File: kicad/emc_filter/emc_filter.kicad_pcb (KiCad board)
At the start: 2 copper layers, 80 x 44 mm, 13 parts

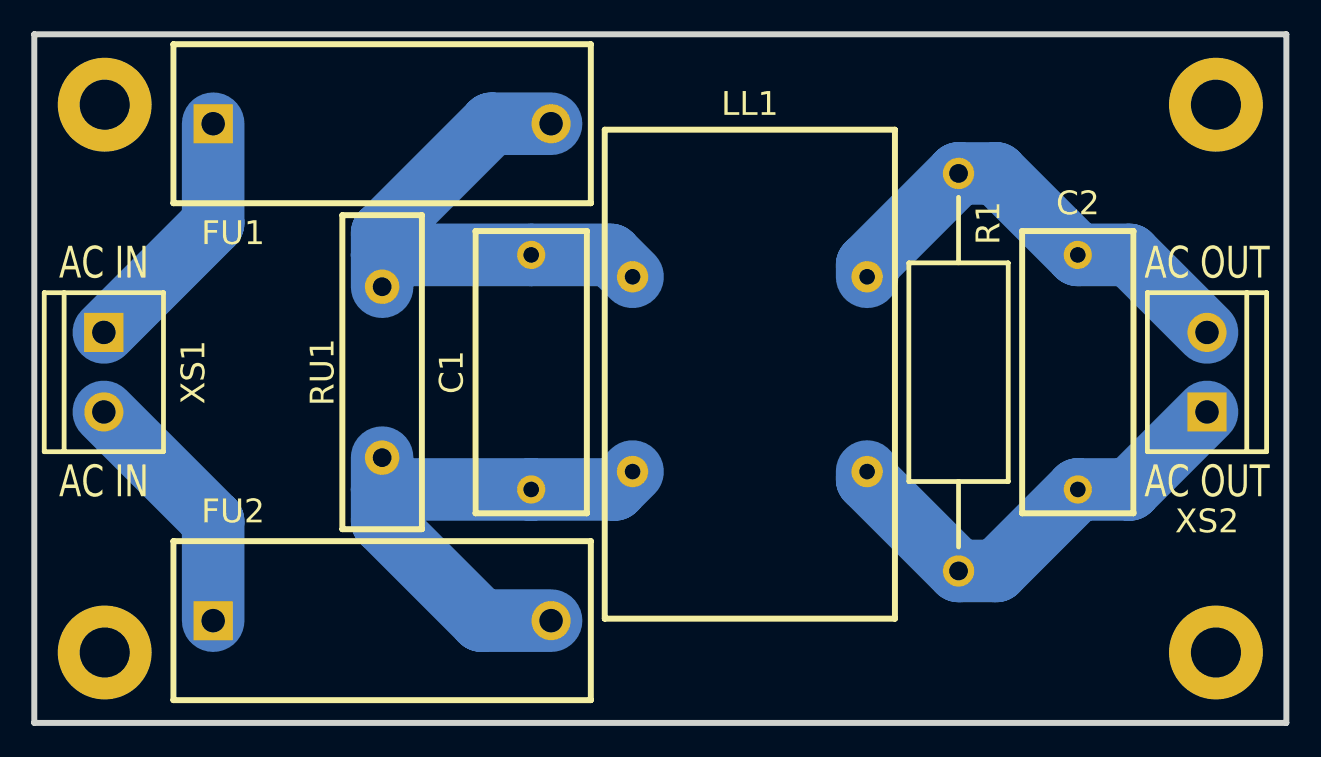
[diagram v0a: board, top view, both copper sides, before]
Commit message: Moved to kicad 4.0.0
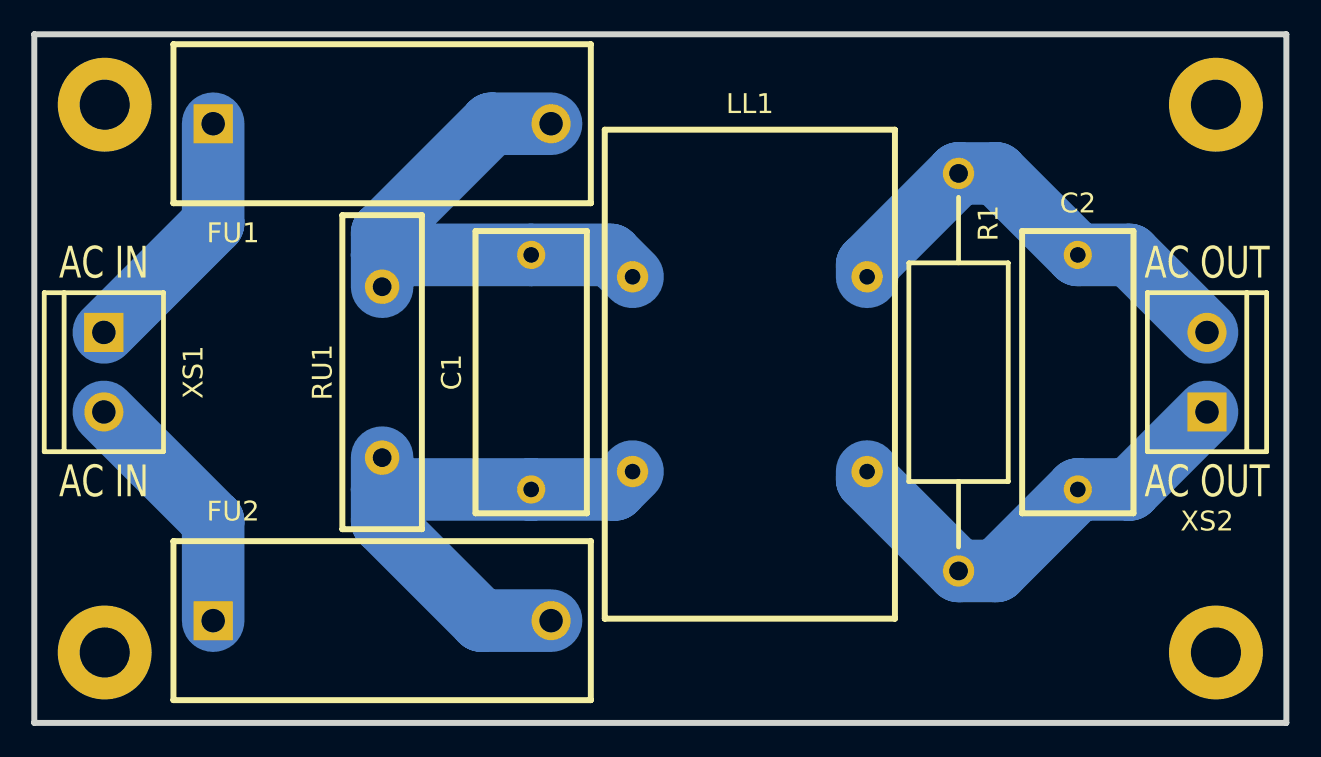
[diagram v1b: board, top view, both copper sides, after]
